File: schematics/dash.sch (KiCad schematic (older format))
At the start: 29 parts, among them J1 BATT_CONN, J2 EXTERNAL_TRIGGER, J3 USB_OTG, SW1 SW_Push, U1 ESP-12E, U2 ch340g, U3 MCP73833, U4 HT7333, Y1 12Mhz

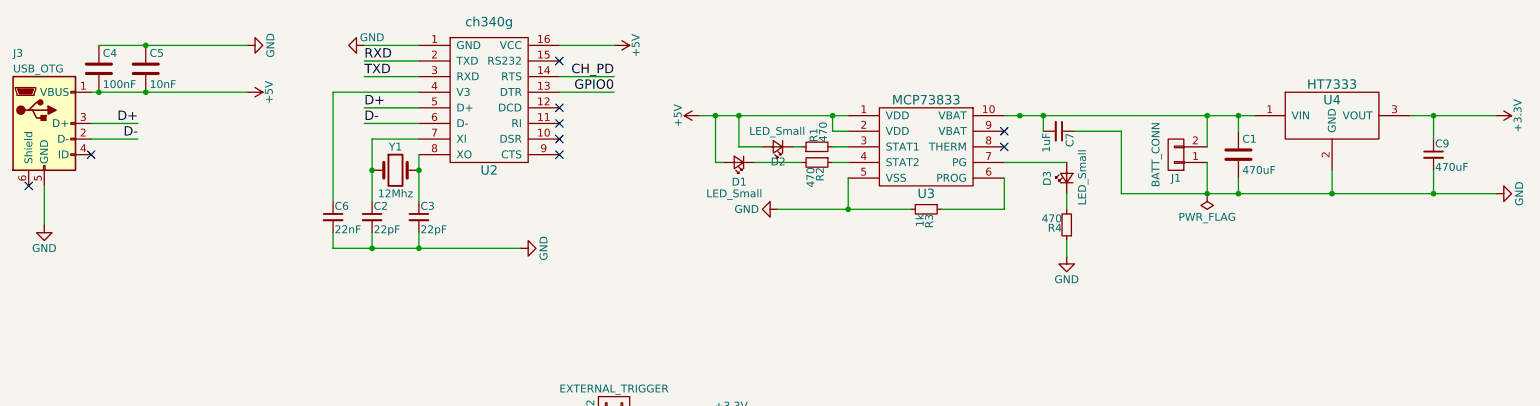
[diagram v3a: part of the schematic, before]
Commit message: [enh] VSS connected directly to the battery
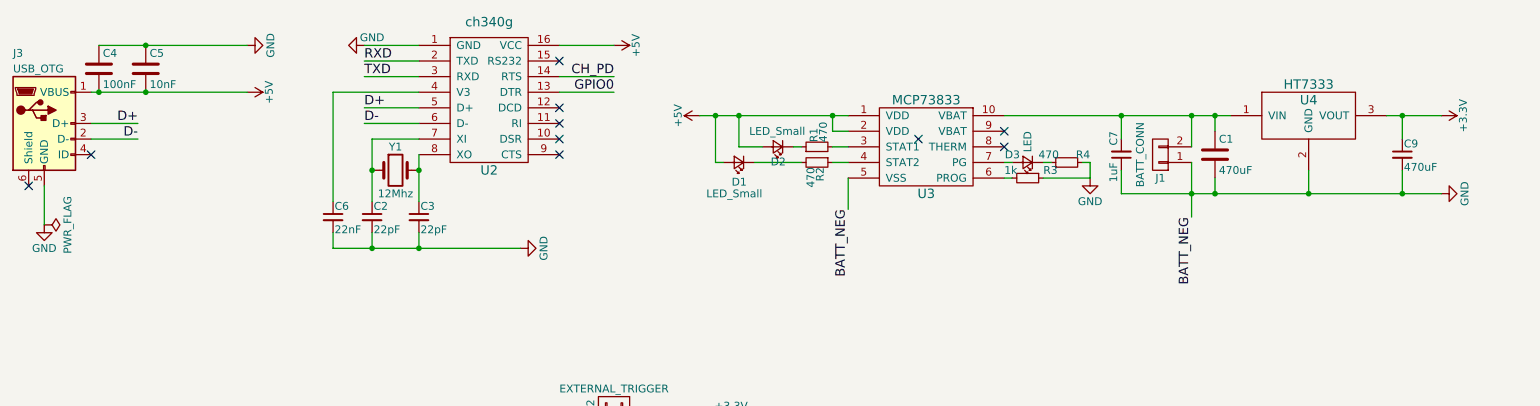
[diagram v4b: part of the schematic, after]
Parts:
- D3: value LED_Small -> LED
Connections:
- net GND: now also R3.1, R4.2; no longer R3.2, R4.1
- net at D3.1 (K): now also R4.1; no longer R4.2
- net at U3.6 (PROG): now also R3.2; no longer R3.1
- no-connect marks 21 -> 22
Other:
- moved on the sheet: C1, C7, C9, D3, J1, R3, R4, U4

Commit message: [add] Shitty design to start with
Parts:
- Y1: footprint Crystals:Crystal_HC49-U_Vertical -> Crystals:Crystal_SMD_2012-2pin_2.0x1.2mm_HandSoldering
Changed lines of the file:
@@
 F 0 "Y1" H 3550 2400 50  0000 C CNN
 F 1 "12Mhz" H 3550 2100 50  0000 C CNN
-F 2 "Crystals:Crystal_HC49-U_Vertical" H 3550 2250 50  0001 C CNN
+F 2 "Crystals:Crystal_SMD_2012-2pin_2.0x1.2mm_HandSoldering" H 3550 2250 50  0001 C CNN
 F 3 "" H 3550 2250 50  0001 C CNN
 	1    3550 2250

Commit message: [fix] Global dependencies to local dependencies (no more path problem)
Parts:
- C7: footprint Capacitors_Tantalum_SMD:Tantalum_Case-A_EIA-3216-18_Hand -> Capacitors_Tantalum_SMD:CP_Tantalum_Case-A_EIA-3216-18_Hand
- C9: footprint Capacitors_Tantalum_SMD:Tantalum_Case-D_EIA-7343-31_Hand -> Capacitors_Tantalum_SMD:CP_Tantalum_Case-D_EIA-7343-31_Hand
- J1: footprint Pin_Headers:Pin_Header_Angled_1x02 -> Connectors_JST:JST_ACH_BM02B-ACHSS_02x1.20mm_Angled
- J2: footprint Pin_Headers:Pin_Header_Straight_1x02 -> Connectors:GS2
- J3: footprint Connect:USB_Micro-B -> Connectors:USB_Micro-B
- SW1: footprint Buttons_Switches_ThroughHole:SW_PUSH_6mm -> Buttons_Switches_SMD:SW_DIP_x1_W5.08mm_Slide_Copal_CHS-A
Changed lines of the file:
@@
 F 0 "SW1" V 5000 4450 50  0000 L CNN
 F 1 "SW_Push" H 4950 4290 50  0000 C CNN
-F 2 "Buttons_Switches_ThroughHole:SW_PUSH_6mm" H 4950 4550 50  0001 C CNN
+F 2 "Buttons_Switches_SMD:SW_DIP_x1_W5.08mm_Slide_Copal_CHS-A" H 4950 4550 50  0001 C CNN
 F 3 "" H 4950 4550 50  0001 C CNN
 	1    4950 4350
@@
 F 0 "J1" H 8450 2300 50  0000 C CNN
 F 1 "BATT_CONN" V 8550 2150 50  0000 C TNN
-F 2 "Pin_Headers:Pin_Header_Angled_1x02" H 8450 2150 50  0001 C CNN
+F 2 "Connectors_JST:JST_ACH_BM02B-ACHSS_02x1.20mm_Angled" H 8450 2150 50  0001 C CNN
 F 3 "" H 8450 2150 50  0001 C CNN
 	1    8450 2150
@@
 F 0 "J2" H 4950 3900 50  0000 C CNN
 F 1 "EXTERNAL_TRIGGER" V 5050 3750 50  0000 C CNN
-F 2 "Pin_Headers:Pin_Header_Straight_1x02" H 4950 3750 50  0001 C CNN
+F 2 "Connectors:GS2" H 4950 3750 50  0001 C CNN
 F 3 "" H 4950 3750 50  0001 C CNN
 	1    4950 3750
@@
 F 0 "J3" H 1100 2400 50  0000 L CNN
 F 1 "USB_OTG" H 1100 2300 50  0000 L CNN
-F 2 "Connect:USB_Micro-B" H 1450 1900 50  0001 C CNN
+F 2 "Connectors:USB_Micro-B" H 1450 1900 50  0001 C CNN
 F 3 "" H 1450 1900 50  0001 C CNN
 	1    1300 1950
@@
 F 0 "C7" V 8250 2000 50  0000 L CNN
 F 1 "1uF" V 8250 2200 50  0000 L CNN
-F 2 "Capacitors_Tantalum_SMD:Tantalum_Case-A_EIA-3216-18_Hand" H 8200 2150 50  0001 C CNN
+F 2 "Capacitors_Tantalum_SMD:CP_Tantalum_Case-A_EIA-3216-18_Hand" H 8200 2150 50  0001 C CNN
 F 3 "" H 8200 2150 50  0001 C CNN
 	1    8200 2150
@@
 F 0 "C9" H 10010 2220 50  0000 L CNN
 F 1 "470uF" H 10010 2070 50  0000 L CNN
-F 2 "Capacitors_Tantalum_SMD:Tantalum_Case-D_EIA-7343-31_Hand" H 10000 2150 50  0001 C CNN
+F 2 "Capacitors_Tantalum_SMD:CP_Tantalum_Case-D_EIA-7343-31_Hand" H 10000 2150 50  0001 C CNN
 F 3 "" H 10000 2150 50  0001 C CNN
 	1    10000 2150

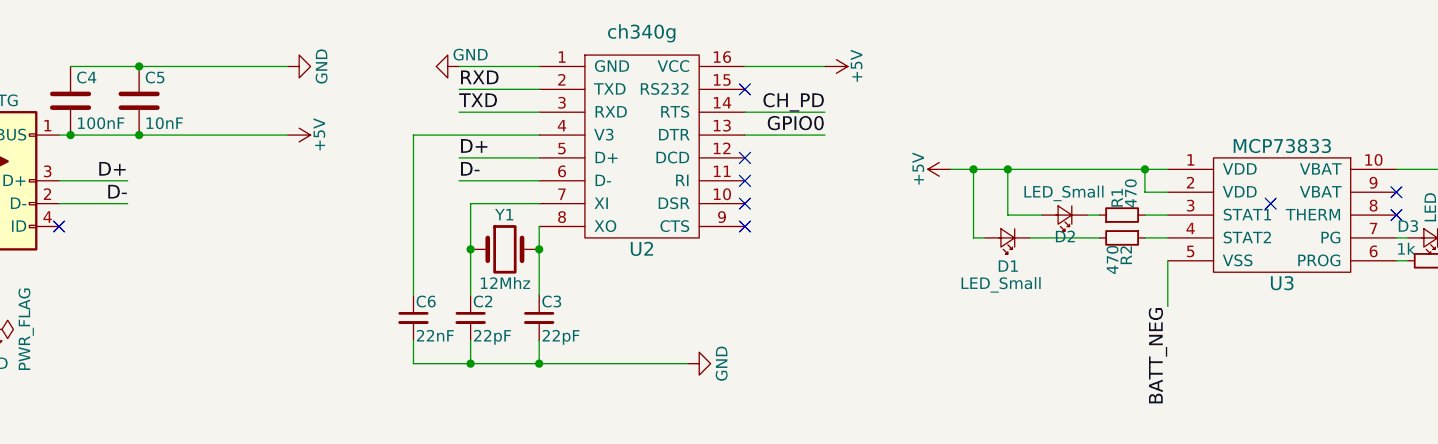
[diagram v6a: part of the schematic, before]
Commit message: [fix] Relative path for the ESP-12 component
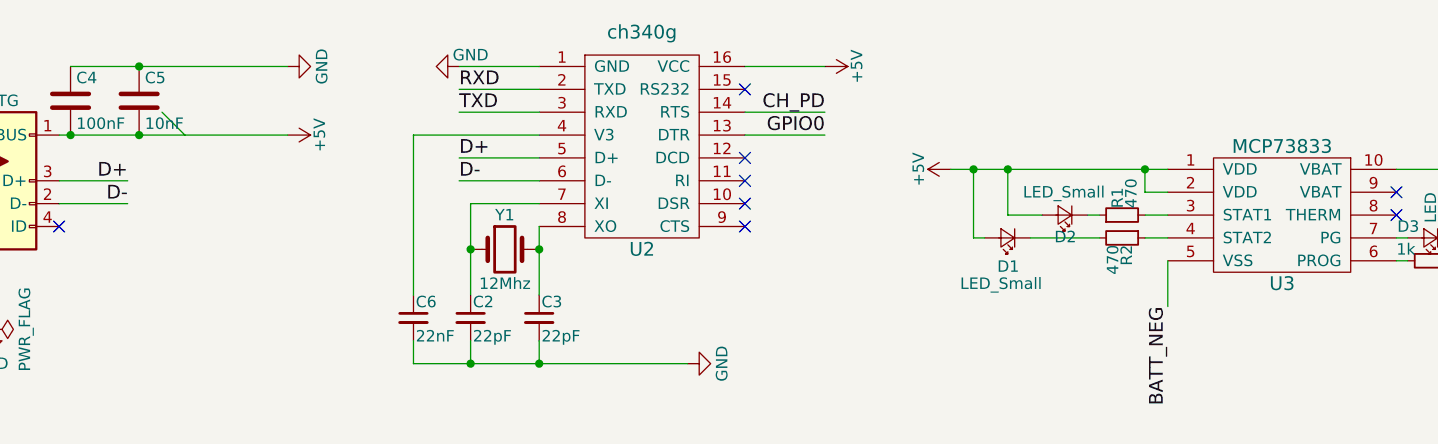
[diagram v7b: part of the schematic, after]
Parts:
- U1: footprint ESP8266:ESP-12E_SMD -> (none)
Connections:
- no-connect marks 22 -> 21
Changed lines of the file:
@@
 EESchema Schematic File Version 2
-LIBS:dash-rescue
 LIBS:power
 LIBS:device
@@
 LIBS:valves
 LIBS:switches
-LIBS:ch340g
+LIBS:ESP8266
 LIBS:dash-cache
 EELAYER 25 0
@@
 Comment4 ""
 $EndDescr
-$Comp
-L ESP-12E U1
-U 1 1 5946DC8B
-P 6650 4650
-F 0 "U1" H 6650 4550 50  0000 C CNN
-F 1 "ESP-12E" H 6650 4750 50  0000 C CNN
-F 2 "ESP8266:ESP-12E_SMD" H 6650 4650 50  0001 C CNN
-F 3 "" H 6650 4650 50  0001 C CNN
-	1    6650 4650
-	1    0    0    -1
-$EndComp
 NoConn ~ 6400 5550
 NoConn ~ 6500 5550
@@
 	5350 4650 5750 4650
 NoConn ~ 7450 2000
-NoConn ~ 6900 2050
 Wire Wire Line
 	7450 2200 7500 2200
@@
 Wire Wire Line
 	9900 1900 10250 1900
+Entry Wire Line
+	2050 1650 2150 1750
+$Comp
+L ESP-12E U1
+U 1 1 59C589B5
+P 6650 4650
+F 0 "U1" H 6650 4550 50  0000 C CNN
+F 1 "ESP-12E" H 6650 4750 50  0000 C CNN
+F 2 "" H 6650 4650 50  0001 C CNN
+F 3 "" H 6650 4650 50  0001 C CNN
+	1    6650 4650
+	1    0    0    -1
+$EndComp
 $EndSCHEMATC

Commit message: [fix] 3DShapes names
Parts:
- U1: footprint (none) -> ESP8266:ESP-12E_SMD
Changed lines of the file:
@@
 F 0 "U1" H 6650 4550 50  0000 C CNN
 F 1 "ESP-12E" H 6650 4750 50  0000 C CNN
-F 2 "" H 6650 4650 50  0001 C CNN
+F 2 "ESP8266:ESP-12E_SMD" H 6650 4650 50  0001 C CNN
 F 3 "" H 6650 4650 50  0001 C CNN
 	1    6650 4650
